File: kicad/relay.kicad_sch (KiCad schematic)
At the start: 8 parts, among them K1 SANYOU_SRD_Form_C, Q2 NPN

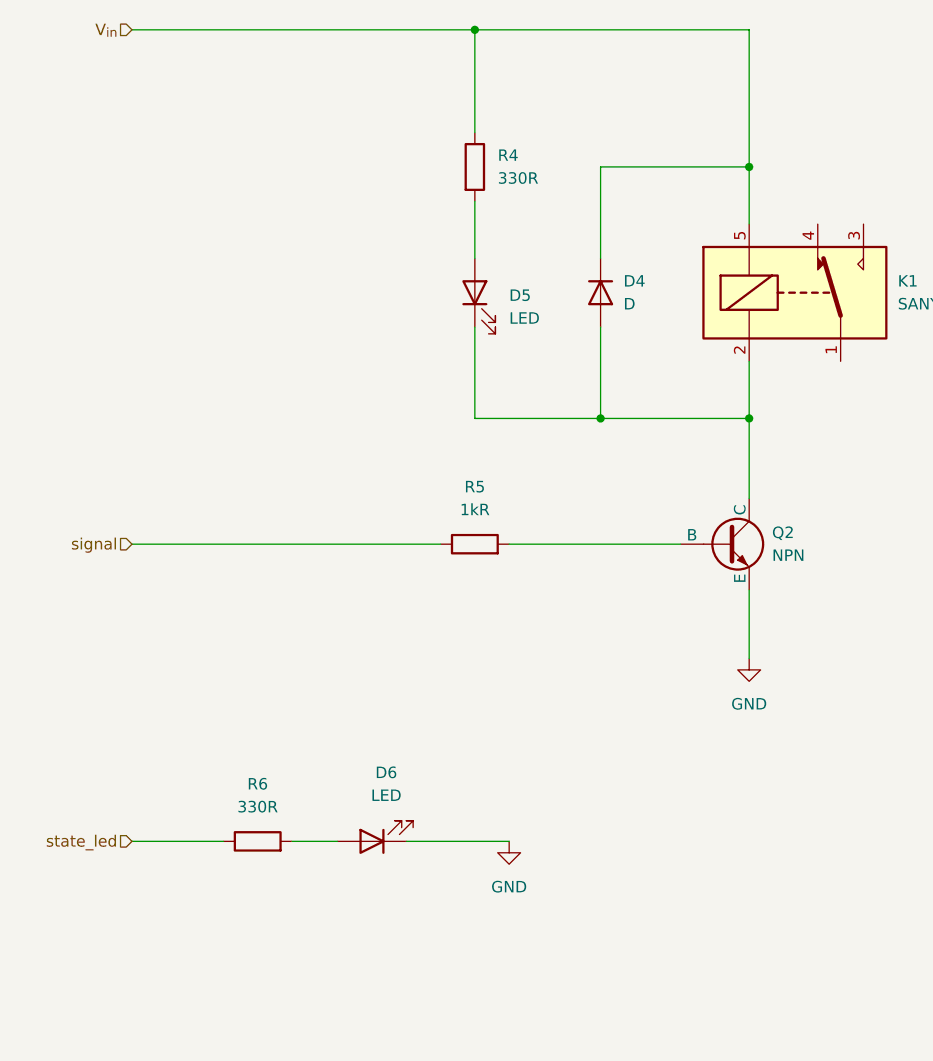
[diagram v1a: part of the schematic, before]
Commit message: aggiunto schema per motori PWM
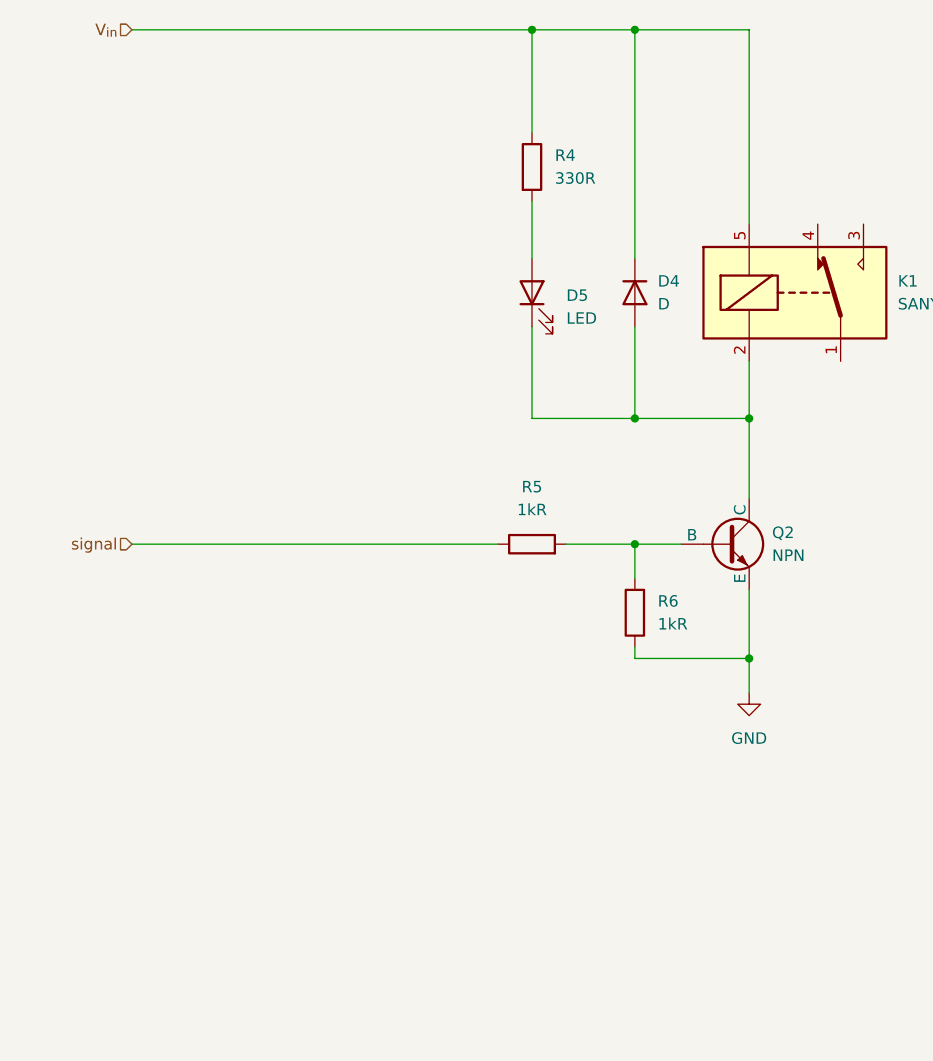
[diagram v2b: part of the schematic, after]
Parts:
- removed D6: LED, symbol Device:LED
- R6: value 330R -> 1kR
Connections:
- net state_led is gone; now on net GND: R6.1
- net at R6.2: now also Q2.2 (B), R5.2
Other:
- moved on the sheet: D4, D5, R4, R5

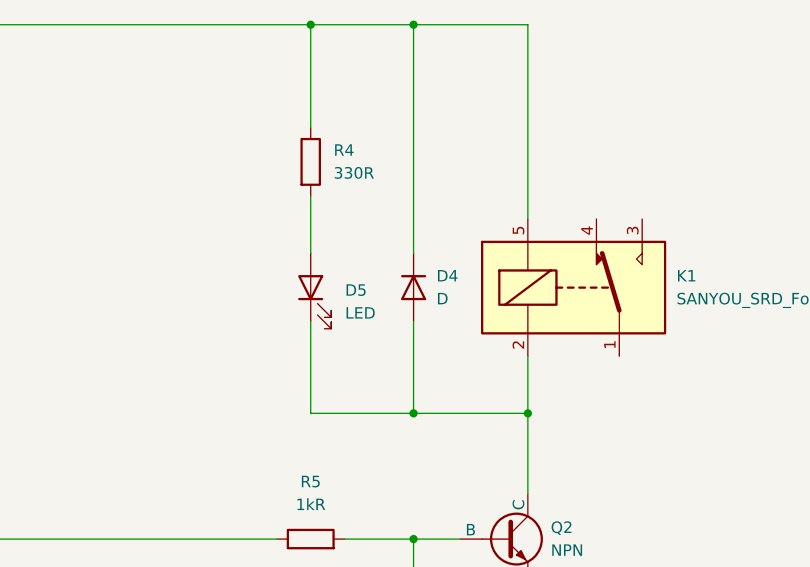
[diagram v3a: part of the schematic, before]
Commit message: terminato collegamento ATMEGA328P
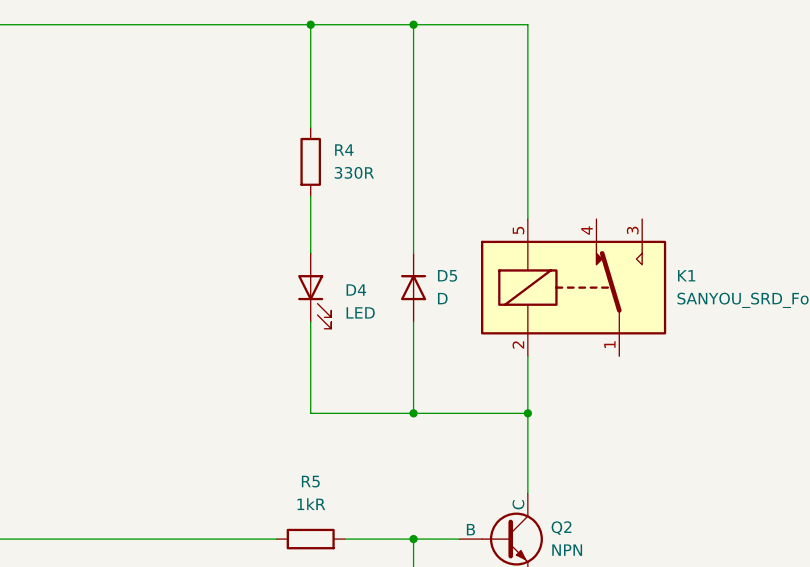
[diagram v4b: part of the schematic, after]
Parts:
- renumbered D5 to D4, D4 to D5
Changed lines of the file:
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@@
 		(dnp no)
 		(fields_autoplaced yes)
-		(property "Reference" "#PWR022"
+		(property "Reference" "#PWR023"
 			(at 38.1 185.42 0)
 			(effects
@@
 			(project "electronics-schemas"
 				(path "/f1ade40e-ee4b-4e00-b57d-44850604005b/292635d8-2cab-4fc1-b7ec-537c82f88846"
-					(reference "#PWR022")
+					(reference "#PWR023")
 					(unit 1)
 				)
@@
 		(dnp no)
 		(fields_autoplaced yes)
-		(property "Reference" "D5"
+		(property "Reference" "D4"
 			(at 77.47 60.0074 90)
 			(effects
@@
 			(project ""
 				(path "/f1ade40e-ee4b-4e00-b57d-44850604005b/292635d8-2cab-4fc1-b7ec-537c82f88846"
-					(reference "D5")
+					(reference "D4")
 					(unit 1)
 				)
@@
 		(dnp no)
 		(fields_autoplaced yes)
-		(property "Reference" "#PWR023"
+		(property "Reference" "#PWR022"
 			(at 97.79 110.49 0)
 			(effects
@@
 			(project "electronics-schemas"
 				(path "/f1ade40e-ee4b-4e00-b57d-44850604005b/292635d8-2cab-4fc1-b7ec-537c82f88846"
-					(reference "#PWR023")
+					(reference "#PWR022")
 					(unit 1)
 				)
@@
 		(dnp no)
 		(fields_autoplaced yes)
-		(property "Reference" "D4"
+		(property "Reference" "D5"
 			(at 87.63 58.4199 90)
 			(effects
@@
 			(project ""
 				(path "/f1ade40e-ee4b-4e00-b57d-44850604005b/292635d8-2cab-4fc1-b7ec-537c82f88846"
-					(reference "D4")
-					(unit 1)
-				)
+					(reference "D5")
+					(unit 1)
+				)
